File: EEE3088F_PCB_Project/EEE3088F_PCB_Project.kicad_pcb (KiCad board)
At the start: 2 copper layers, 6 parts, among them IC1 DRV8833PWPR, IC2 DRV8833PWPR, IC3 TPS62067DSGR, IC4 TPS62067DSGR, IC5 INA219AIDCNR, J1 Conn_02x16_Odd_Even

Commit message: v1.2
Starting with PCB design
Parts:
- removed IC4: TPS62067DSGR, TPS62067DSGR KiCad:SON50P200X200X80-9N
- added J3: Conn_01x02, Connector_JST:JST_PH_S2B-PH-K_1x02_P2.00mm_Horizontal, F.Cu at (165.5, 96.0)
- added Q1: AO3400A, AO3400A KiCad:SOT95P280X125-3N, F.Cu at (79.2, 57.7)
- added Q2: AO3400A, AO3400A KiCad:SOT95P280X125-3N, F.Cu at (79.2, 62.4)
- added Q5: AO3401A, AO3400A KiCad:SOT95P280X125-3N, F.Cu at (143.5, 88.0)
- added Q6: AO3401A, AO3400A KiCad:SOT95P280X125-3N, F.Cu at (149.0, 88.0)
- added U3: IRLML6344TRPBF, IRLML6344TRPBF:IRLML6344TRPBF_INF, F.Cu at (84.2, 57.9)
- J1: footprint Connector_Samtec_HLE_THT:Samtec_HLE-116-02-xx-DV-TE_2x16_P2.54mm_Horizontal -> Connector_PinSocket_2.54mm:PinSocket_2x16_P2.54mm_Vertical; moved to B.Cu
- moved IC5 68.8 mm to (84.5, 63.3)
- moved IC3 63.9 mm to (84.0, 67.7), turned to 0 degrees
- moved J1 37.5 mm to (159.3, 98.5), turned to 90 degrees
- moved IC2 11.1 mm to (142.6, 94.3)
- moved IC1 10.9 mm to (134.6, 94.2)
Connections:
- IC3 pad 5: /BATTERY -> Net-(IC3-AVIN)
- IC3 pad 6: GND -> /PWR SWITCH OUT
- IC3 pad 7: /BATTERY -> Net-(IC3-AVIN)
- IC3 pad 8: /BATTERY -> Net-(IC3-AVIN)
- IC5 pad 4: /3V3 OUT -> Net-(IC5-VS)
- J1 pad 15: /RESV -> unconnected-(J1-Pin_15-Pad15)
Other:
- board outline added: 77.3 x 53 mm

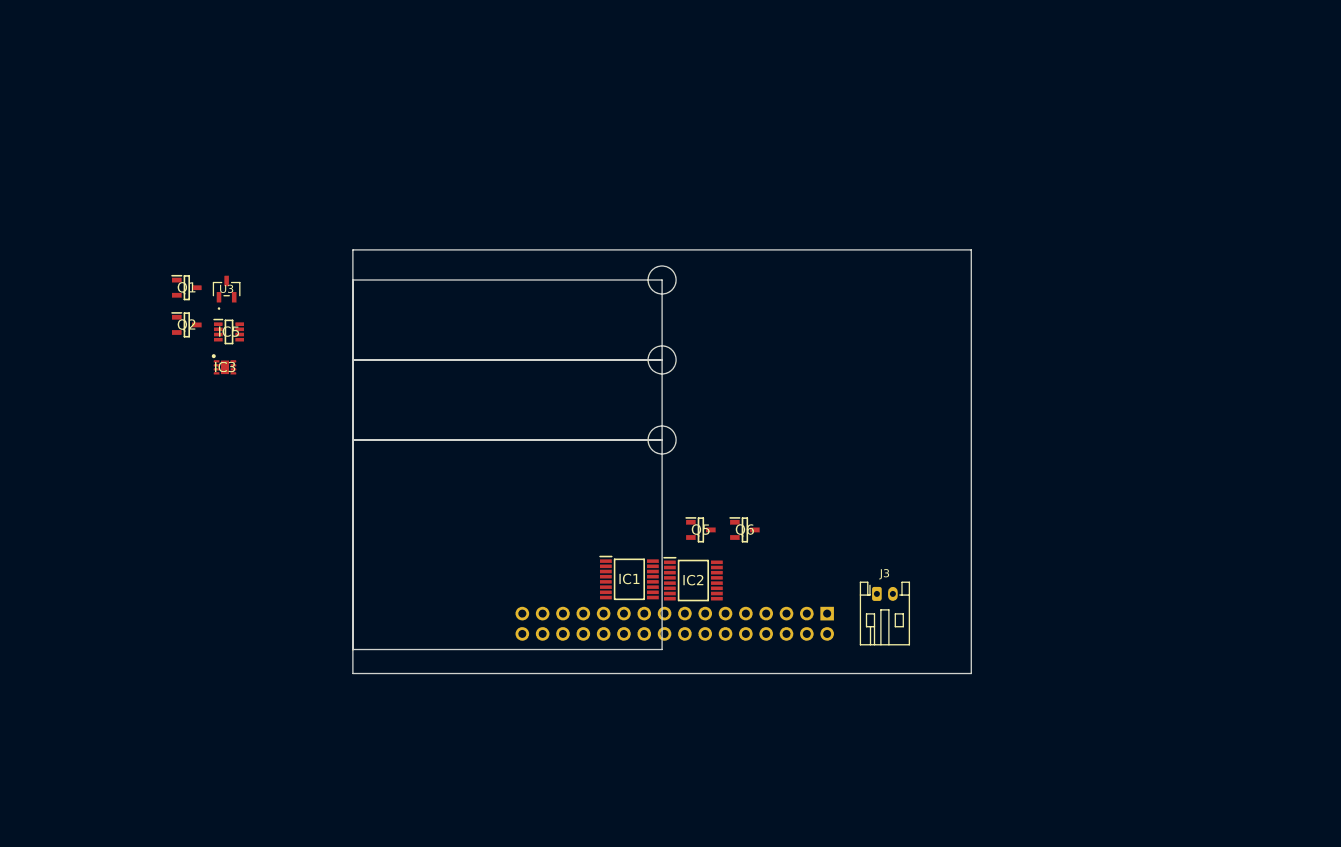
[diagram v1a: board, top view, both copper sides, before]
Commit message: v1.2.2
Footprints added
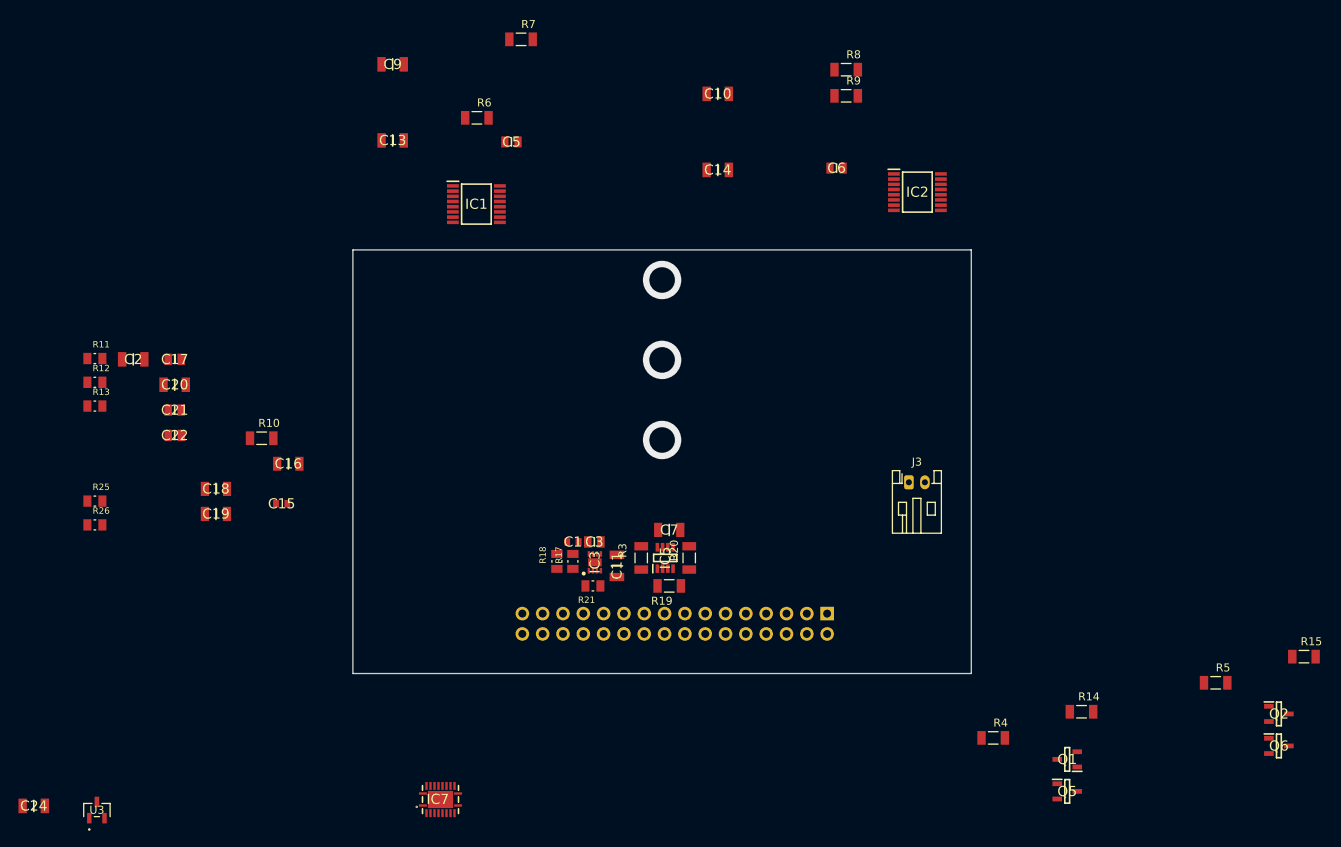
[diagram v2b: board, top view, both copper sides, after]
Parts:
- added C1: 10p, CL10C100JB8NNNC KiCad:CAPC1608X90N, F.Cu at (127.5, 89.5)
- added C10: 10µ, CL31A106KBHNNNE KiCad:CAPC3216X180N, F.Cu at (145.6, 33.5)
- added C11: 10µ, CL31A106KBHNNNE KiCad:CAPC3216X180N, F.Cu at (133.0, 92.5)
- added C13: 2.2µ, CL31B225KBHNNNE KiCad:CAPC3216X180N, F.Cu at (105.0, 39.3)
- added C14: 2.2µ, CL31B225KBHNNNE KiCad:CAPC3216X180N, F.Cu at (145.6, 43.0)
- added C15: 47n, CL10B473KB8NNNC KiCad:CAPC1608X90N, F.Cu at (91.1, 84.7)
- added C16: 1n, 1206B102K202NT KiCad:CAPC3215X163N, F.Cu at (91.9, 79.7)
- added C17: 22µ, CL21A226MAQNNNE KiCad:CAPC2012X140N, F.Cu at (77.7, 66.7)
- added C18: 100n, CL31B104KBCNNNC KiCad:CAPC3216X100N, F.Cu at (82.9, 82.9)
- added C19: 100n, CL31B104KBCNNNC KiCad:CAPC3216X100N, F.Cu at (82.9, 86.0)
- added C2: 2.2µ, CL31B225KBHNNNE KiCad:CAPC3216X180N, F.Cu at (72.5, 66.7)
- added C20: 10µ, CL31A106KBHNNNE KiCad:CAPC3216X180N, F.Cu at (77.7, 69.8)
- added C21: 22µ, CL21A226MAQNNNE KiCad:CAPC2012X140N, F.Cu at (77.7, 73.0)
- added C22: 22µ, CL21A226MAQNNNE KiCad:CAPC2012X140N, F.Cu at (77.7, 76.2)
- added C24: 10u, CL31A106KBHNNNE KiCad:CAPC3216X180N, F.Cu at (60.1, 122.5)
- added C3: 22µ, CL21A226MAQNNNE KiCad:CAPC2012X140N, F.Cu at (130.2, 89.5)
- added C5: 10n, CL21B103KBANNNC KiCad:CAPC2012X75N, F.Cu at (119.8, 39.5)
- added C6: 10n, CL21B103KBANNNC KiCad:CAPC2012X75N, F.Cu at (160.5, 42.8)
- added C7: 100n, CL31B104KBCNNNC KiCad:CAPC3216X100N, F.Cu at (139.5, 88.0)
- added C9: 10µ, CL31A106KBHNNNE KiCad:CAPC3216X180N, F.Cu at (105.0, 29.8)
- added IC7: TPS61088RHLR, TPS61088RHLR KiCad:RHL_R-PVQFN-N20__1, F.Cu at (111.0, 121.7)
- added R10: 100k, 1206W4F1003T5E:RESC3115X65N, F.Cu at (88.6, 76.5)
- added R11: 47k, 0805W8F4702T5E:RESC2012X65N, F.Cu at (67.7, 66.6)
- added R12: 220k, 0805W8F2203T5E:RESC2012X65N, F.Cu at (67.7, 69.5)
- added R13: 150k, 0805W8F1503T5E:RESC2012X65N, F.Cu at (67.7, 72.5)
- added R14: 100, 1206W4F1000T5E:RESC3115X65N, F.Cu at (191.1, 110.7)
- added R15: 100, 1206W4F1000T5E:RESC3115X65N, F.Cu at (218.9, 103.8)
- added R17: 220k, 0805W8F2203T5E:RESC2012X65N, F.Cu at (127.5, 91.9)
- added R18: 470k, 0805W8F4703T5E:RESC2012X65N, F.Cu at (125.5, 91.9)
- added R19: 50m, 1206W3F500MT5E:RESC3115X65N, F.Cu at (139.5, 95.0)
- added R20: 4k7, 1206W4F4701T5E:RESC3115X65N, F.Cu at (142.0, 91.5)
- added R21: 150k, 0805W8F1503T5E:RESC2012X65N, F.Cu at (130.0, 95.0)
- added R25: 33k, 0805W8F3302T5E:RESC2012X65N, F.Cu at (67.7, 84.4)
- added R26: 68k, 0805W8F6802T5E:RESC2012X65N, F.Cu at (67.7, 87.4)
- added R3: 4k7, 1206W4F4701T5E:RESC3115X65N, F.Cu at (136.0, 91.5)
- added R4: 1M, 1206W4F1004T5E:RESC3115X65N, F.Cu at (180.0, 114.0)
- added R5: 1M, 1206W4F1004T5E:RESC3115X65N, F.Cu at (207.8, 107.1)
- added R6: 1, 1206W4F100KT5E:RESC3115X65N, F.Cu at (115.5, 36.5)
- added R7: 1, 1206W4F100KT5E:RESC3115X65N, F.Cu at (121.0, 26.7)
- added R8: 400m, 1206W4F400LT5E:RESC3115X65N, F.Cu at (161.7, 30.5)
- added R9: 400m, 1206W4F400LT5E:RESC3115X65N, F.Cu at (161.7, 33.7)
- Q5, Q6: footprint AO3400A KiCad:SOT95P280X125-3N -> AO3401A KiCad:SOT95P280X125-3N
- moved Q2 144.9 mm to (215.8, 111.0)
- moved Q1 124.8 mm to (189.3, 116.7), turned to 180 degrees
- moved Q6 72.0 mm to (215.8, 115.0)
- moved U3 67.1 mm to (68.0, 123.0)
- moved IC5 61.4 mm to (139.0, 91.5), turned to 90 degrees
- moved Q5 56.3 mm to (189.3, 120.7)
- moved IC2 56.0 mm to (170.6, 45.8)
- moved IC3 52.3 mm to (130.2, 92.0), turned to 90 degrees
- moved IC1 50.6 mm to (115.4, 47.3)
- moved J3 14.5 mm to (169.5, 82.0)
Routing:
- net (no net): vias 0 -> 3
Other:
- outline, holes or cut-outs redrawn

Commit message: v1.3
Lula: all my footprints imported and circuits grouped on PCB
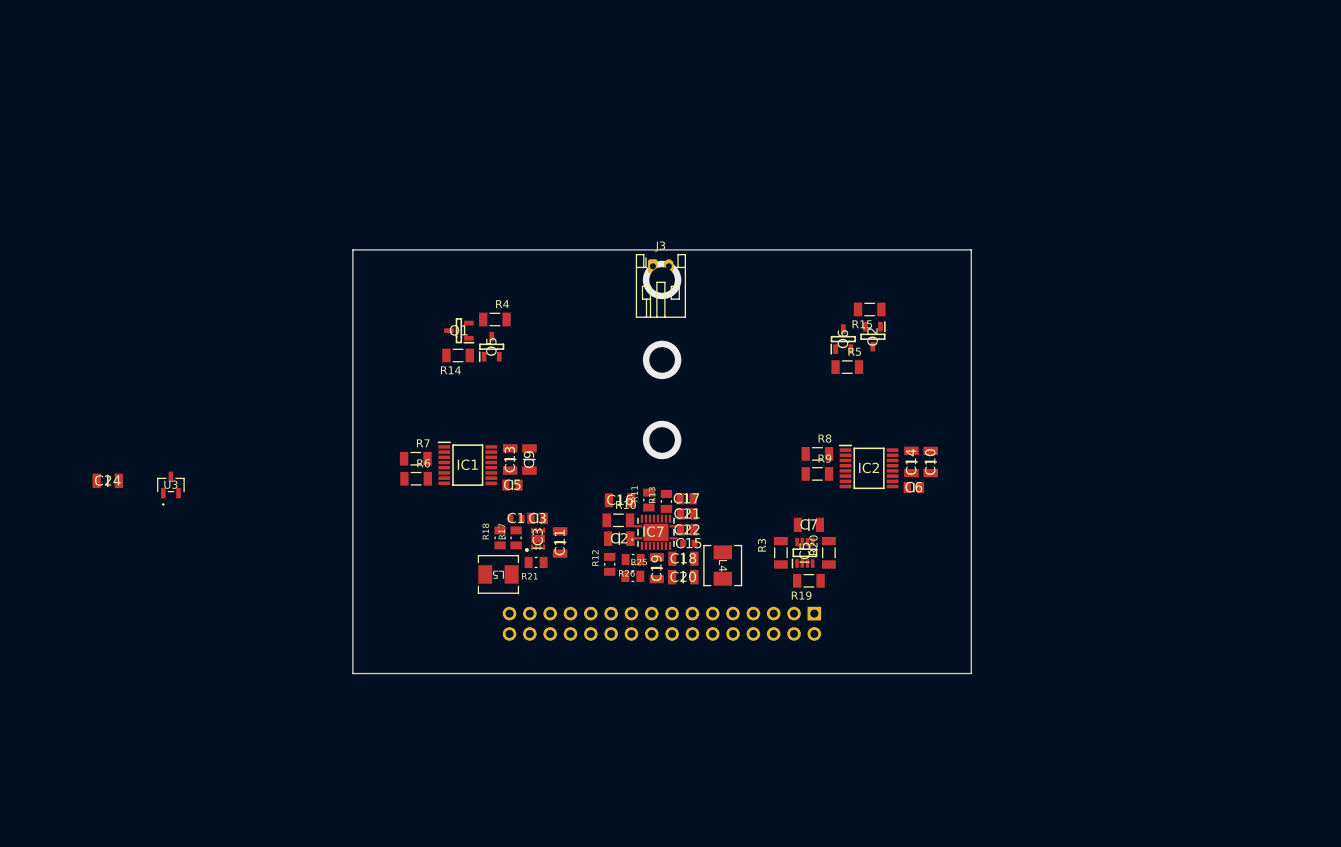
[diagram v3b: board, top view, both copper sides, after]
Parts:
- added L4: 1.2µ, FXL0420-1R2-M KiCADv6:IND_FXL0420_CMT, F.Cu at (146.2, 92.5)
- added L5: 1.2µ, FXL0420-1R2-M KiCADv6:IND_FXL0420_CMT, F.Cu at (118.2, 93.6)
- moved Q1 93.0 mm to (113.2, 63.1)
- moved Q5 90.9 mm to (117.3, 65.1), turned to 90 degrees
- moved R14 89.8 mm to (113.2, 66.2), turned to 180 degrees
- moved R4 81.3 mm to (117.8, 61.7)
- moved Q6 74.5 mm to (161.3, 64.2), turned to 90 degrees
- moved R13 72.4 mm to (139.2, 84.4), turned to 90 degrees
- moved R11 71.5 mm to (137.0, 84.3), turned to 90 degrees
- moved R15 69.5 mm to (164.6, 60.5), turned to 180 degrees
- moved Q2 69.3 mm to (165.0, 63.9), turned to -90 degrees
- moved R12 68.3 mm to (132.1, 92.3), turned to 90 degrees
- moved C20 68.0 mm to (141.3, 93.9)
- moved R25 67.9 mm to (135.0, 93.8)
- moved R26 67.4 mm to (135.0, 91.7), turned to 180 degrees
- moved C17 66.3 mm to (141.7, 84.1)
- moved C21 65.4 mm to (141.8, 86.0)
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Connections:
- J3 pad 1: /BATTERY -> GND
- J3 pad 2: GND -> /BATTERY

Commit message: v1.3.1
Most components placed on PCB
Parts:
- added J2: TYPE-C16PIN, TYPE-C16PIN KiCADv6:CONN16_C16PIN_SHN, F.Cu at (108.1, 97.1)
- added L2: 2u2, FHW0805UF2R2JST:L0805, F.Cu at (135.0, 71.1)
- added LED1: 0805G (Green), KT-0805G:LED0805-R-RD, F.Cu at (124.2, 69.7)
- added LED2: KT-0603R, KT-0603R:LED0603-RD, F.Cu at (124.6, 66.6)
- added R16: 5k6, R0402:R0402, F.Cu at (126.3, 74.8)
- added R27: 3k3, R0402:R0402, F.Cu at (128.5, 75.2)
- added R28: 1k, R0402:R0402, F.Cu at (135.0, 73.8)
- added R29: 75k, 0603WAF7502T5E:R0603, F.Cu at (125.2, 123.7)
- added R30: 1k, R0402:R0402, F.Cu at (126.6, 68.3)
- added SW1: 1MS1T1B1M2QES, 1MS1TIB1M2QES KiCADv6:1MS1T1_DYW, F.Cu at (146.8, 65.7)
- added TP1: TestPoint, TestPoint:TestPoint_2Pads_Pitch2.54mm_Drill0.8mm, F.Cu at (108.8, 84.1)
- added TP2: TestPoint, TestPoint:TestPoint_2Pads_Pitch2.54mm_Drill0.8mm, F.Cu at (155.9, 81.3)
- added U2: SLM6600, SL6600 KiCad:SOP8_4X5P1-1P27_SOI, F.Cu at (129.9, 71.6)
- moved C24 62.3 mm to (129.9, 67.4)
- moved U3 49.7 mm to (126.7, 77.6)
- moved J3 6.31 mm to (131.2, 55.4)
- moved C10 2.44 mm to (171.4, 77.2)
- moved C6 2.44 mm to (169.3, 80.4)
- moved IC2 2.44 mm to (163.7, 78.0)
- moved R8 2.44 mm to (157.3, 76.2)
- moved R9 2.44 mm to (157.3, 78.7)
- moved C14 2.44 mm to (169.0, 77.2)

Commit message: V1.4.1
last minute things
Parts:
- moved J2 62.8 mm to (158.8, 60.0), turned to 0 degrees
- moved R29 50.9 mm to (145.2, 76.8)
- moved C9 16.6 mm to (107.3, 71.5), turned to 180 degrees
- moved C13 13.4 mm to (107.3, 74.0), turned to 0 degrees
- moved C5 12.9 mm to (110.5, 73.7), turned to 90 degrees
- moved C7 7.91 mm to (164.9, 86.9)
- moved IC5 7.91 mm to (164.4, 90.4)
- moved R19 7.91 mm to (164.9, 93.9)
- moved R20 7.91 mm to (167.4, 90.4)
- moved R3 7.91 mm to (161.4, 90.4)
- moved R7 6.68 mm to (107.2, 85.8), turned to 90 degrees
- moved IC1 6.39 mm to (108.0, 79.2), turned to 90 degrees
- moved R14 5.68 mm to (108.8, 62.5)
- moved R4 5.68 mm to (113.4, 58.0)
- moved Q1 5.68 mm to (108.9, 59.5)
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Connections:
- J2 pad A8: unconnected-(J2-SBU1-PadA8) -> Net-(J2-SBU1)
- J2 pad B8: unconnected-(J2-SBU2-PadB8) -> Net-(J2-SBU2)
- R27 pad 1: Net-(U3-S) -> Net-(Q3-S)
